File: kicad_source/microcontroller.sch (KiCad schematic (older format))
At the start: 42 parts, among them CN1 Micro_SDCard, CN2 CONN_02X05, SW1 TAST_VER, SW2 TAST_VER, SW3 TAST_VER, SW4 TAST_VER, U1 W25Q80D, U2 ATECC608A, U3 FE310-G002, Y1 16MHz

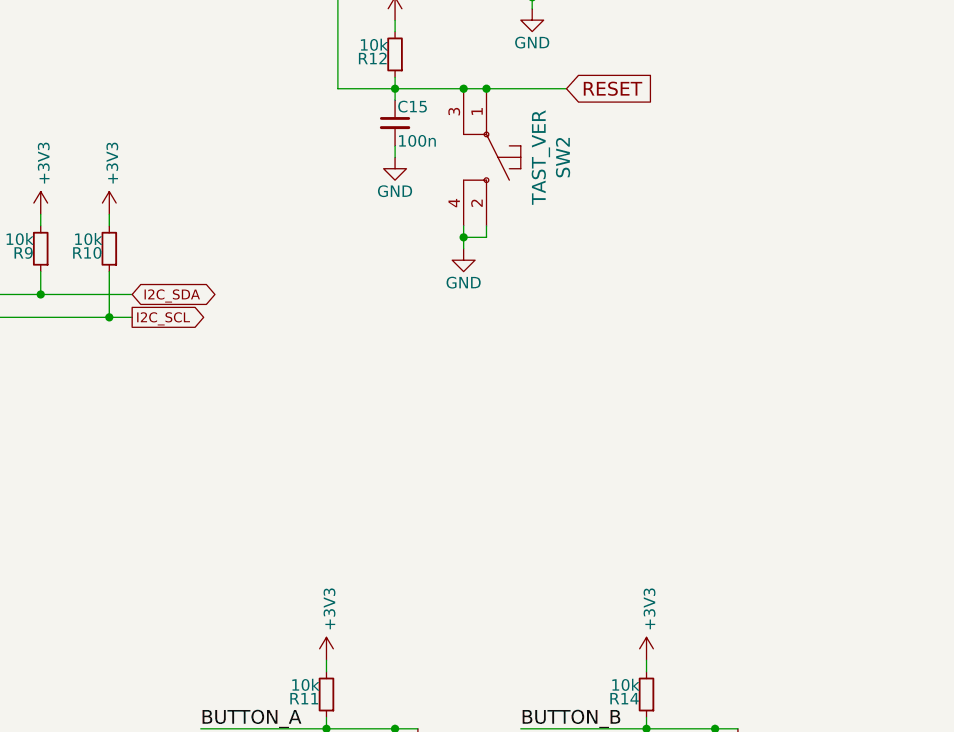
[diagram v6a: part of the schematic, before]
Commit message: added qwiic connector for I2C and grove connector for UART
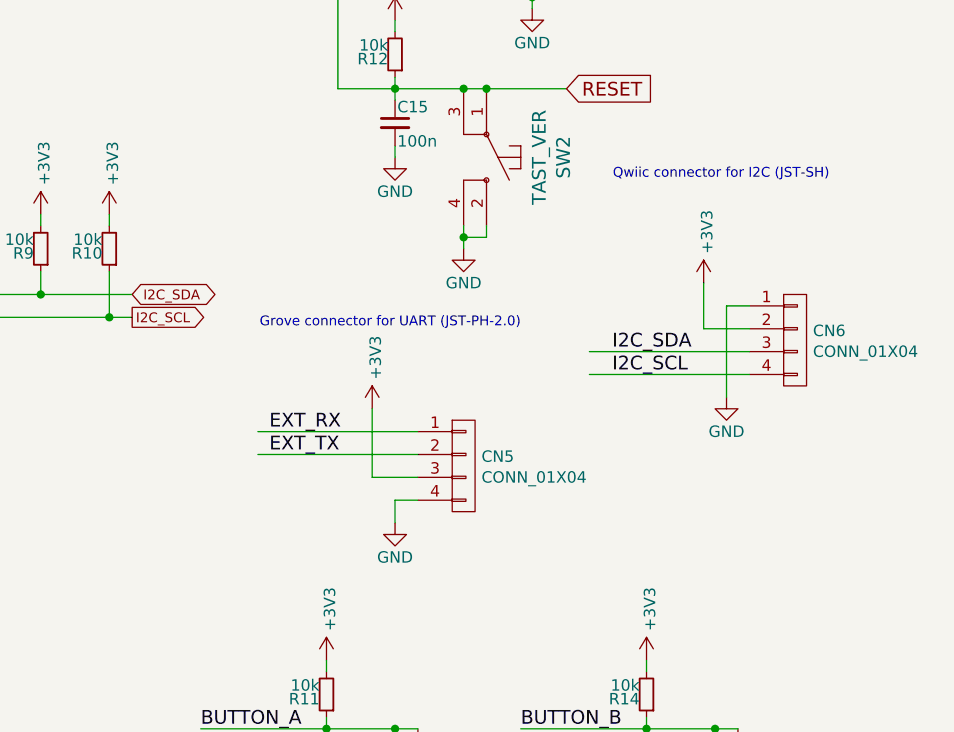
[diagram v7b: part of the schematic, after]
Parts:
- added CN5: CONN_01X04, connectors_JST_PH:Connectors_JST_S4B-PH-SM4-TB, symbol mechanical-connectors:CONN_01X04
- added CN6: CONN_01X04, connectors_JST_SH:Connectors_JST_SM04B-SRSS-TB, symbol mechanical-connectors:CONN_01X04
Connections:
- wire segments 209 -> 221
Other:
- note added: "Grove connector for UART (JST-PH-2.0)"
- note added: "Qwiic connector for I2C (JST-SH)"
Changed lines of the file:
@@
 Wire Wire Line
 	5250 5400 5250 5350
+$Comp
+L mechanical-connectors:CONN_01X04 CN6
+U 1 1 5EBDD3B1
+P 10850 3800
+F 0 "CN6" H 10928 3841 50  0000 L CNN
+F 1 "CONN_01X04" H 10928 3750 50  0000 L CNN
+F 2 "connectors_JST_SH:Connectors_JST_SM04B-SRSS-TB" H 10850 3800 50  0001 C CNN
+F 3 "" H 10850 3800 50  0000 C CNN
+	1    10850 3800
+	1    0    0    -1
+$EndComp
+$Comp
+L power-supply:+3V3 #PWR089
+U 1 1 5EBDD791
+P 10450 3550
+F 0 "#PWR089" H 10450 3400 50  0001 C CNN
+F 1 "+3V3" V 10465 3678 50  0000 L CNN
+F 2 "" H 10450 3550 50  0000 C CNN
+F 3 "" H 10450 3550 50  0000 C CNN
+	1    10450 3550
+	1    0    0    -1
+$EndComp
+$Comp
+L power-supply:GND #PWR090
+U 1 1 5EBDDC2C
+P 10550 4050
+F 0 "#PWR090" H 10550 3800 50  0001 C CNN
+F 1 "GND" H 10550 3900 50  0000 C CNN
+F 2 "" H 10550 4050 50  0000 C CNN
+F 3 "" H 10550 4050 50  0000 C CNN
+	1    10550 4050
+	1    0    0    -1
+$EndComp
+Wire Wire Line
+	10650 3650 10550 3650
+Wire Wire Line
+	10550 3650 10550 4050
+Wire Wire Line
+	10650 3750 10450 3750
+Wire Wire Line
+	10450 3750 10450 3550
+Wire Wire Line
+	9950 3850 10650 3850
+Wire Wire Line
+	9950 3950 10650 3950
+Text Label 10050 3850 0    60   ~ 0
+I2C_SDA
+Text Label 10050 3950 0    60   ~ 0
+I2C_SCL
+Text Notes 11000 3100 2    43   ~ 0
+Qwiic connector for I2C (JST-SH)
+$Comp
+L mechanical-connectors:CONN_01X04 CN5
+U 1 1 5EC139A4
+P 9400 4350
+F 0 "CN5" H 9478 4391 50  0000 L CNN
+F 1 "CONN_01X04" H 9478 4300 50  0000 L CNN
+F 2 "connectors_JST_PH:Connectors_JST_S4B-PH-SM4-TB" H 9478 4254 50  0001 L CNN
+F 3 "" H 9400 4350 50  0000 C CNN
+	1    9400 4350
+	1    0    0    -1
+$EndComp
+$Comp
+L power-supply:+3V3 #PWR087
+U 1 1 5EC139AE
+P 9000 4100
+F 0 "#PWR087" H 9000 3950 50  0001 C CNN
+F 1 "+3V3" V 9015 4228 50  0000 L CNN
+F 2 "" H 9000 4100 50  0000 C CNN
+F 3 "" H 9000 4100 50  0000 C CNN
+	1    9000 4100
+	1    0    0    -1
+$EndComp
+$Comp
+L power-supply:GND #PWR088
+U 1 1 5EC139B8
+P 9100 4600
+F 0 "#PWR088" H 9100 4350 50  0001 C CNN
+F 1 "GND" H 9100 4450 50  0000 C CNN
+F 2 "" H 9100 4600 50  0000 C CNN
+F 3 "" H 9100 4600 50  0000 C CNN
+	1    9100 4600
+	1    0    0    -1
+$EndComp
+Wire Wire Line
+	8500 4200 9200 4200
+Wire Wire Line
+	8500 4300 9200 4300
+Wire Wire Line
+	9200 4400 9000 4400
+Wire Wire Line
+	9000 4400 9000 4100
+Wire Wire Line
+	9200 4500 9100 4500
+Wire Wire Line
+	9100 4500 9100 4600
+Text Label 8550 4200 0    60   ~ 0
+EXT_RX
+Text Label 8550 4300 0    60   ~ 0
+EXT_TX
+Text Notes 9650 3750 2    43   ~ 0
+Grove connector for UART (JST-PH-2.0)
 $EndSCHEMATC

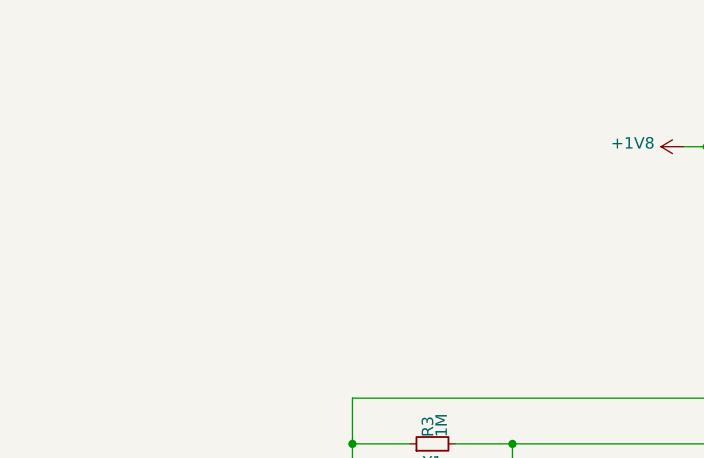
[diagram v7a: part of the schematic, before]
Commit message: added BMA400 accelerometer
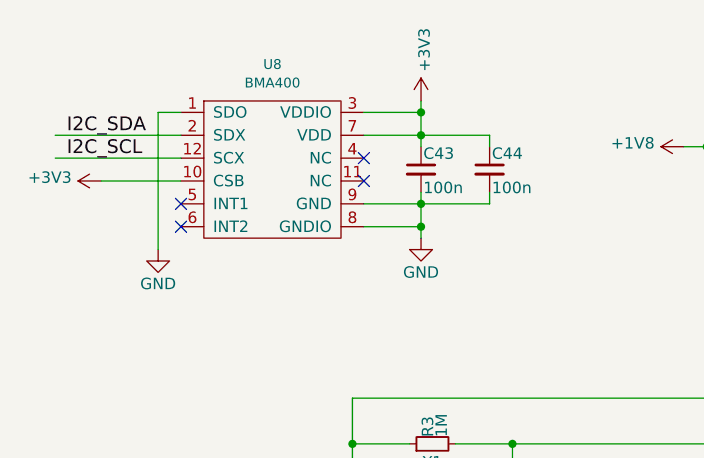
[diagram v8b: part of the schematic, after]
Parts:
- added C43, C44: 100n, capacitors:C_0603, symbol devices:C_0603
- added U8: BMA400, IC_sensor:BMA400, symbol IC_sensor:BMA400
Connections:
- wire segments 221 -> 240
- no-connect marks 9 -> 13
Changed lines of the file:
@@
 Text Notes 9650 3750 2    43   ~ 0
 Grove connector for UART (JST-PH-2.0)
+$Comp
+L IC_sensor:BMA400 U8
+U 1 1 5EBEEA8A
+P 1650 1300
+F 0 "U8" H 1650 1760 43  0000 C CNN
+F 1 "BMA400" H 1650 1679 43  0000 C CNN
+F 2 "IC_sensor:BMA400" H 1650 1300 43  0001 C CNN
+F 3 "" H 1650 1300 43  0001 C CNN
+	1    1650 1300
+	1    0    0    -1
+$EndComp
+$Comp
+L devices:C_0603 C43
+U 1 1 5EBEF994
+P 2300 1300
+F 0 "C43" H 2310 1370 50  0000 L CNN
+F 1 "100n" H 2310 1220 50  0000 L CNN
+F 2 "capacitors:C_0603" H 2300 1150 50  0001 C CNN
+F 3 "" H 2300 1300 50  0000 C CNN
+	1    2300 1300
+	1    0    0    -1
+$EndComp
+$Comp
+L power-supply:GND #PWR094
+U 1 1 5EBEFDAB
+P 2300 1600
+F 0 "#PWR094" H 2300 1350 50  0001 C CNN
+F 1 "GND" H 2300 1450 50  0000 C CNN
+F 2 "" H 2300 1600 50  0000 C CNN
+F 3 "" H 2300 1600 50  0000 C CNN
+	1    2300 1600
+	1    0    0    -1
+$EndComp
+$Comp
+L power-supply:+3V3 #PWR093
+U 1 1 5EBF023A
+P 2300 1000
+F 0 "#PWR093" H 2300 850 50  0001 C CNN
+F 1 "+3V3" V 2315 1128 50  0000 L CNN
+F 2 "" H 2300 1000 50  0000 C CNN
+F 3 "" H 2300 1000 50  0000 C CNN
+	1    2300 1000
+	1    0    0    -1
+$EndComp
+Wire Wire Line
+	2300 1600 2300 1550
+Wire Wire Line
+	2050 1450 2300 1450
+Connection ~ 2300 1450
+Wire Wire Line
+	2300 1450 2300 1400
+Wire Wire Line
+	2050 1550 2300 1550
+Connection ~ 2300 1550
+Wire Wire Line
+	2300 1550 2300 1450
+Wire Wire Line
+	2300 1200 2300 1150
+Wire Wire Line
+	2050 1050 2300 1050
+Connection ~ 2300 1050
+Wire Wire Line
+	2300 1050 2300 1000
+Wire Wire Line
+	2050 1150 2300 1150
+Connection ~ 2300 1150
+Wire Wire Line
+	2300 1150 2300 1050
+NoConn ~ 2050 1250
+NoConn ~ 2050 1350
+NoConn ~ 1250 1450
+NoConn ~ 1250 1550
+$Comp
+L power-supply:GND #PWR092
+U 1 1 5EC77215
+P 1150 1650
+F 0 "#PWR092" H 1150 1400 50  0001 C CNN
+F 1 "GND" H 1150 1500 50  0000 C CNN
+F 2 "" H 1150 1650 50  0000 C CNN
+F 3 "" H 1150 1650 50  0000 C CNN
+	1    1150 1650
+	1    0    0    -1
+$EndComp
+Wire Wire Line
+	1250 1050 1150 1050
+Wire Wire Line
+	1150 1050 1150 1650
+$Comp
+L power-supply:+3V3 #PWR091
+U 1 1 5EC8591C
+P 900 1350
+F 0 "#PWR091" H 900 1200 50  0001 C CNN
+F 1 "+3V3" V 915 1478 50  0000 L CNN
+F 2 "" H 900 1350 50  0000 C CNN
+F 3 "" H 900 1350 50  0000 C CNN
+	1    900  1350
+	0    -1   -1   0
+$EndComp
+Wire Wire Line
+	1250 1350 900  1350
+Wire Wire Line
+	700  1250 1250 1250
+Wire Wire Line
+	700  1150 1250 1150
+Text Label 750  1150 0    60   ~ 0
+I2C_SDA
+Text Label 750  1250 0    60   ~ 0
+I2C_SCL
+$Comp
+L devices:C_0603 C44
+U 1 1 5ECB7E97
+P 2600 1300
+F 0 "C44" H 2610 1370 50  0000 L CNN
+F 1 "100n" H 2610 1220 50  0000 L CNN
+F 2 "capacitors:C_0603" H 2600 1150 50  0001 C CNN
+F 3 "" H 2600 1300 50  0000 C CNN
+	1    2600 1300
+	1    0    0    -1
+$EndComp
+Wire Wire Line
+	2600 1200 2600 1150
+Wire Wire Line
+	2600 1150 2300 1150
+Wire Wire Line
+	2600 1400 2600 1450
+Wire Wire Line
+	2600 1450 2300 1450
 $EndSCHEMATC
